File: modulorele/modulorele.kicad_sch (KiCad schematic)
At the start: 9 parts, among them J1 Rele, J2 Conn_01x03, K1 G5LE-1, Q1 SS8050

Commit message: Some changes in arduino board.
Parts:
- removed J1: Rele, TerminalBlock_Phoenix:TerminalBlock_Phoenix_MKDS-1,5-3-5.08_1x03_P5.08mm_Horizontal, symbol Connector:Screw_Terminal_01x03
- removed J2: Conn_01x03, Connector_PinHeader_2.54mm:PinHeader_1x03_P2.54mm_Vertical, symbol Connector_Generic:Conn_01x03
- added J15: Conn_01x01, Connector_PinHeader_2.54mm:PinHeader_1x01_P2.54mm_Vertical, symbol Connector_Generic:Conn_01x01
- added JP3: ~, Jumper:SolderJumper-2_P1.3mm_Bridged_RoundedPad1.0x1.5mm, symbol Jumper:SolderJumper_2_Bridged
- renumbered D1 to D5, D2 to D6, Q1 to Q3, R3 to R13, R2 to R14, R1 to R15
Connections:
- net at R13.1, R15.1: now also JP3.2 (B)
- net +12V renamed 12V
- net com renamed COM
- net na renamed NA
- net nf renamed NF
- new net INPUT: J15.1 (Pin_1), JP3.1 (A)

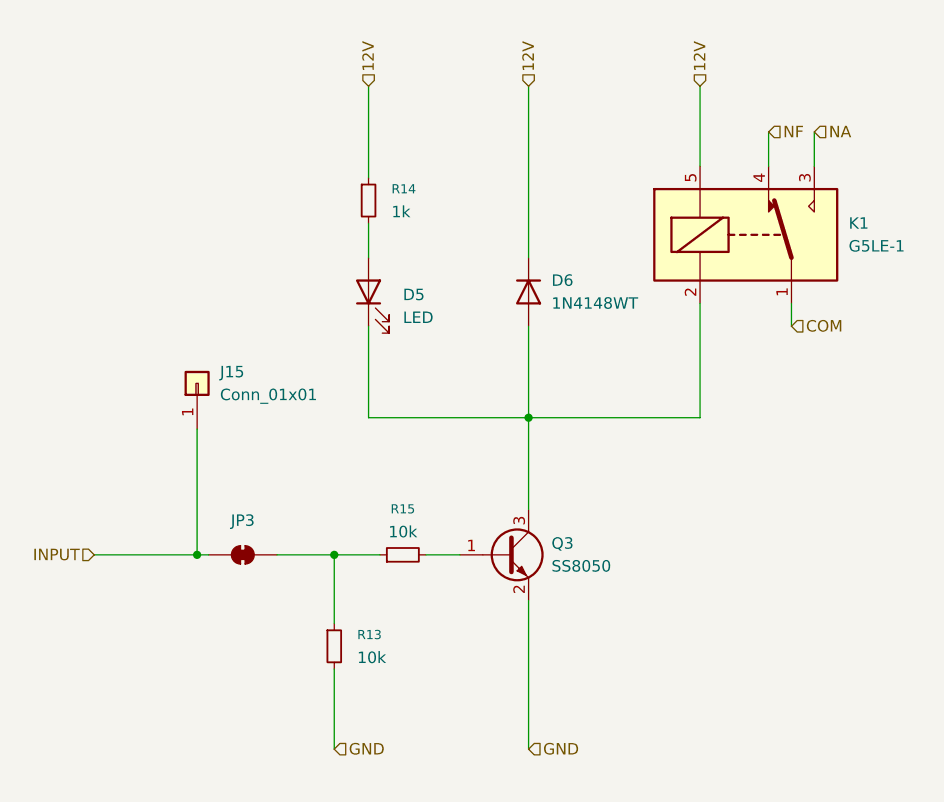
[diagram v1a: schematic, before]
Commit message: Added all components to arduino pcb.
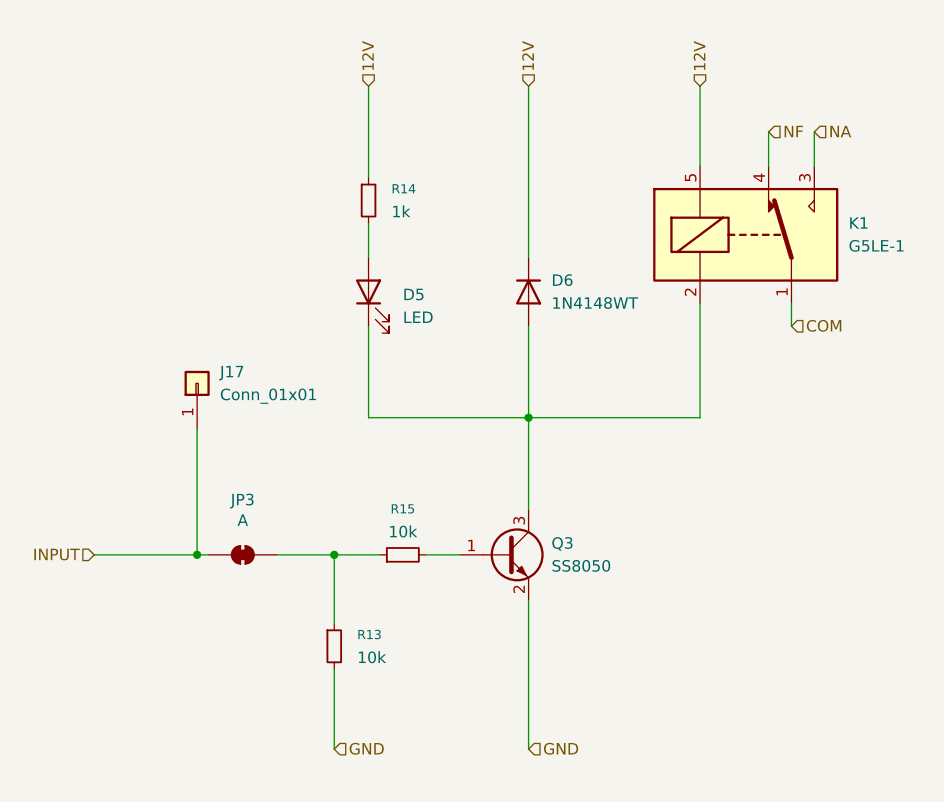
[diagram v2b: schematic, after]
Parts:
- JP3: value ~ -> A
- R13, R14, R15: footprint Resistor_SMD:R_0805_2012Metric -> Resistor_SMD:R_0805_2012Metric_Pad1.20x1.40mm_HandSolder
- renumbered J15 to J17
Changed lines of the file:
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@@
 		(dnp no)
 		(fields_autoplaced yes)
-		(property "Reference" "J15"
+		(property "Reference" "J17"
 			(at 57.15 66.0399 90)
 			(effects
@@
 			(project "Arduino"
 				(path "/b1260de1-9c48-4b08-a759-f31e40d6183e/6d409481-8893-4a65-ac5a-8215d51ff4b9/2c4cc56f-8712-443e-bcef-d2b6de1486c0"
+					(reference "J19")
+					(unit 1)
+				)
+				(path "/b1260de1-9c48-4b08-a759-f31e40d6183e/6d409481-8893-4a65-ac5a-8215d51ff4b9/4a654f2d-0a20-4954-8c37-0a9e1e731e6d"
+					(reference "J18")
+					(unit 1)
+				)
+				(path "/b1260de1-9c48-4b08-a759-f31e40d6183e/6d409481-8893-4a65-ac5a-8215d51ff4b9/7c0386ab-ad55-49ca-9208-412e4006b70e"
 					(reference "J17")
 					(unit 1)
 				)
-				(path "/b1260de1-9c48-4b08-a759-f31e40d6183e/6d409481-8893-4a65-ac5a-8215d51ff4b9/4a654f2d-0a20-4954-8c37-0a9e1e731e6d"
-					(reference "J16")
-					(unit 1)
-				)
-				(path "/b1260de1-9c48-4b08-a759-f31e40d6183e/6d409481-8893-4a65-ac5a-8215d51ff4b9/7c0386ab-ad55-49ca-9208-412e4006b70e"
-					(reference "J15")
-					(unit 1)
-				)
-				(path "/b1260de1-9c48-4b08-a759-f31e40d6183e/6d409481-8893-4a65-ac5a-8215d51ff4b9/cd925d39-8883-46ed-ba4c-9b4976049c05"
-					(reference "J18")
+				(path "/b1260de1-9c48-4b08-a759-f31e40d6183e/6d409481-8893-4a65-ac5a-8215d51ff4b9/cd925d39-8883-46ed-ba4c-9b4976049c05"
+					(reference "J26")
 					(unit 1)
 				)
@@
 			)
 		)
-		(property "Footprint" "Resistor_SMD:R_0805_2012Metric"
+		(property "Footprint" "Resistor_SMD:R_0805_2012Metric_Pad1.20x1.40mm_HandSolder"
 			(at 69.85 96.52 0)
 			(effects
@@
 				)
 				(path "/b1260de1-9c48-4b08-a759-f31e40d6183e/6d409481-8893-4a65-ac5a-8215d51ff4b9/cd925d39-8883-46ed-ba4c-9b4976049c05"
-					(reference "R22")
+					(reference "R28")
 					(unit 1)
 				)
@@
 				)
 				(path "/b1260de1-9c48-4b08-a759-f31e40d6183e/6d409481-8893-4a65-ac5a-8215d51ff4b9/cd925d39-8883-46ed-ba4c-9b4976049c05"
-					(reference "D11")
+					(reference "D15")
 					(unit 1)
 				)
@@
 			)
 		)
-		(property "Footprint" "Resistor_SMD:R_0805_2012Metric"
+		(property "Footprint" "Resistor_SMD:R_0805_2012Metric_Pad1.20x1.40mm_HandSolder"
 			(at 77.47 86.36 0)
 			(effects
@@
 				)
 				(path "/b1260de1-9c48-4b08-a759-f31e40d6183e/6d409481-8893-4a65-ac5a-8215d51ff4b9/cd925d39-8883-46ed-ba4c-9b4976049c05"
-					(reference "R24")
+					(reference "R30")
 					(unit 1)
 				)
@@
 				)
 				(path "/b1260de1-9c48-4b08-a759-f31e40d6183e/6d409481-8893-4a65-ac5a-8215d51ff4b9/cd925d39-8883-46ed-ba4c-9b4976049c05"
-					(reference "D12")
+					(reference "D16")
 					(unit 1)
 				)
@@
 		(dnp no)
 		(property "Reference" "JP3"
-			(at 59.69 82.55 0)
-			(effects
-				(font
-					(size 1.27 1.27)
-				)
-			)
-		)
-		(property "Value" "~"
+			(at 59.69 80.264 0)
+			(effects
+				(font
+					(size 1.27 1.27)
+				)
+			)
+		)
+		(property "Value" "A"
 			(at 59.69 82.55 0)
 			(effects
@@
 				)
 				(path "/b1260de1-9c48-4b08-a759-f31e40d6183e/6d409481-8893-4a65-ac5a-8215d51ff4b9/cd925d39-8883-46ed-ba4c-9b4976049c05"
-					(reference "JP6")
+					(reference "JP10")
 					(unit 1)
 				)
@@
 			)
 		)
-		(property "Footprint" "Resistor_SMD:R_0805_2012Metric"
+		(property "Footprint" "Resistor_SMD:R_0805_2012Metric_Pad1.20x1.40mm_HandSolder"
 			(at 73.66 46.99 0)
 			(effects
@@
 				)
 				(path "/b1260de1-9c48-4b08-a759-f31e40d6183e/6d409481-8893-4a65-ac5a-8215d51ff4b9/cd925d39-8883-46ed-ba4c-9b4976049c05"
-					(reference "R23")
-					(unit 1)
-				)
+					(reference "R29")
+					(unit 1)
+				)

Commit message: First version from PCB schematic.
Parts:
- removed D6: 1N4148WT, Diode_SMD:D_SOD-523, symbol Diode:1N4148WT
- added D6: 1N4007, Diode_SMD:D_SMA, symbol Diode:1N4007
- renumbered JP3 to JP4
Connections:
- net at D5.1 (K), K1.2, Q3.3 (C): now also D6.2 (A)
- net 12V renamed +12V
- net +12V: now also D6.1 (K)
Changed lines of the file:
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@@
 		)
 	)
-	(hierarchical_label "12V"
+	(hierarchical_label "+12V"
 		(shape input)
 		(at 110.49 34.29 90)
@@
 		)
 	)
-	(hierarchical_label "12V"
+	(hierarchical_label "+12V"
 		(shape input)
 		(at 73.66 34.29 90)
@@
 		)
 	)
-	(hierarchical_label "12V"
+	(hierarchical_label "+12V"
 		(shape input)
 		(at 91.44 34.29 90)
@@
 					(unit 1)
 				)
-				(path "/b1260de1-9c48-4b08-a759-f31e40d6183e/6d409481-8893-4a65-ac5a-8215d51ff4b9/7c0386ab-ad55-49ca-9208-412e4006b70e"
+				(path "/b1260de1-9c48-4b08-a759-f31e40d6183e/6d409481-8893-4a65-ac5a-8215d51ff4b9/95d6ed7c-668f-45ec-9d3e-e04d0bc610f9"
 					(reference "J17")
 					(unit 1)
@@
 					(unit 1)
 				)
-				(path "/b1260de1-9c48-4b08-a759-f31e40d6183e/6d409481-8893-4a65-ac5a-8215d51ff4b9/7c0386ab-ad55-49ca-9208-412e4006b70e"
+				(path "/b1260de1-9c48-4b08-a759-f31e40d6183e/6d409481-8893-4a65-ac5a-8215d51ff4b9/95d6ed7c-668f-45ec-9d3e-e04d0bc610f9"
 					(reference "R13")
 					(unit 1)
@@
 					(unit 1)
 				)
-				(path "/b1260de1-9c48-4b08-a759-f31e40d6183e/6d409481-8893-4a65-ac5a-8215d51ff4b9/7c0386ab-ad55-49ca-9208-412e4006b70e"
+				(path "/b1260de1-9c48-4b08-a759-f31e40d6183e/6d409481-8893-4a65-ac5a-8215d51ff4b9/95d6ed7c-668f-45ec-9d3e-e04d0bc610f9"
 					(reference "D5")
 					(unit 1)
@@
 				(path "/b1260de1-9c48-4b08-a759-f31e40d6183e/6d409481-8893-4a65-ac5a-8215d51ff4b9/cd925d39-8883-46ed-ba4c-9b4976049c05"
 					(reference "D15")
+					(unit 1)
+				)
+			)
+		)
+	)
+	(symbol
+		(lib_id "Diode:1N4007")
+		(at 91.44 57.15 270)
+		(unit 1)
+		(exclude_from_sim no)
+		(in_bom yes)
+		(on_board yes)
+		(dnp no)
+		(fields_autoplaced yes)
+		(property "Reference" "D6"
+			(at 93.98 55.8799 90)
+			(effects
+				(font
+					(size 1.27 1.27)
+				)
+				(justify left)
+			)
+		)
+		(property "Value" "1N4007"
+			(at 93.98 58.4199 90)
+			(effects
+				(font
+					(size 1.27 1.27)
+				)
+				(justify left)
+			)
+		)
+		(property "Footprint" "Diode_SMD:D_SMA"
+			(at 86.995 57.15 0)
+			(effects
+				(font
+					(size 1.27 1.27)
+				)
+				(hide yes)
+			)
+		)
+		(property "Datasheet" "http://www.vishay.com/docs/88503/1n4001.pdf"
+			(at 91.44 57.15 0)
+			(effects
+				(font
+					(size 1.27 1.27)
+				)
+				(hide yes)
+			)
+		)
+		(property "Description" "1000V 1A General Purpose Rectifier Diode, DO-41"
+			(at 91.44 57.15 0)
+			(effects
+				(font
+					(size 1.27 1.27)
+				)
+				(hide yes)
+			)
+		)
+		(property "Sim.Device" "D"
+			(at 91.44 57.15 0)
+			(effects
+				(font
+					(size 1.27 1.27)
+				)
+				(hide yes)
+			)
+		)
+		(property "Sim.Pins" "1=K 2=A"
+			(at 91.44 57.15 0)
+			(effects
+				(font
+					(size 1.27 1.27)
+				)
+				(hide yes)
+			)
+		)
+		(pin "2"
+		)
+		(pin "1"
+		)
+		(instances
+			(project "Arduino"
+				(path "/b1260de1-9c48-4b08-a759-f31e40d6183e/6d409481-8893-4a65-ac5a-8215d51ff4b9/2c4cc56f-8712-443e-bcef-d2b6de1486c0"
+					(reference "D10")
+					(unit 1)
+				)
+				(path "/b1260de1-9c48-4b08-a759-f31e40d6183e/6d409481-8893-4a65-ac5a-8215d51ff4b9/4a654f2d-0a20-4954-8c37-0a9e1e731e6d"
+					(reference "D8")
+					(unit 1)
+				)
+				(path "/b1260de1-9c48-4b08-a759-f31e40d6183e/6d409481-8893-4a65-ac5a-8215d51ff4b9/95d6ed7c-668f-45ec-9d3e-e04d0bc610f9"
+					(reference "D6")
+					(unit 1)
+				)
+				(path "/b1260de1-9c48-4b08-a759-f31e40d6183e/6d409481-8893-4a65-ac5a-8215d51ff4b9/cd925d39-8883-46ed-ba4c-9b4976049c05"
+					(reference "D16")
 					(unit 1)
 				)
@@
 					(unit 1)
 				)
-				(path "/b1260de1-9c48-4b08-a759-f31e40d6183e/6d409481-8893-4a65-ac5a-8215d51ff4b9/7c0386ab-ad55-49ca-9208-412e4006b70e"
+				(path "/b1260de1-9c48-4b08-a759-f31e40d6183e/6d409481-8893-4a65-ac5a-8215d51ff4b9/95d6ed7c-668f-45ec-9d3e-e04d0bc610f9"
 					(reference "Q3")
 					(unit 1)
@@
 					(unit 1)
 				)
-				(path "/b1260de1-9c48-4b08-a759-f31e40d6183e/6d409481-8893-4a65-ac5a-8215d51ff4b9/7c0386ab-ad55-49ca-9208-412e4006b70e"
+				(path "/b1260de1-9c48-4b08-a759-f31e40d6183e/6d409481-8893-4a65-ac5a-8215d51ff4b9/95d6ed7c-668f-45ec-9d3e-e04d0bc610f9"
 					(reference "R15")
 					(unit 1)
@@
 				(path "/b1260de1-9c48-4b08-a759-f31e40d6183e/6d409481-8893-4a65-ac5a-8215d51ff4b9/cd925d39-8883-46ed-ba4c-9b4976049c05"
 					(reference "R30")
-					(unit 1)
-				)
-			)
-		)
-	)
-	(symbol
-		(lib_id "Diode:1N4148WT")
-		(at 91.44 57.15 270)
-		(unit 1)
-		(exclude_from_sim no)
-		(in_bom yes)
-		(on_board yes)
-		(dnp no)
-		(fields_autoplaced yes)
-		(property "Reference" "D6"
-			(at 93.98 55.8799 90)
-			(effects
-				(font
-					(size 1.27 1.27)
-				)
-				(justify left)
-			)
-		)
-		(property "Value" "1N4148WT"
-			(at 93.98 58.4199 90)
-			(effects
-				(font
-					(size 1.27 1.27)
-				)
-				(justify left)
-			)
-		)
-		(property "Footprint" "Diode_SMD:D_SOD-523"
-			(at 86.995 57.15 0)
-			(effects
-				(font
-					(size 1.27 1.27)
-				)
-				(hide yes)
-			)
-		)
-		(property "Datasheet" "https://www.diodes.com/assets/Datasheets/ds30396.pdf"
-			(at 91.44 57.15 0)
-			(effects
-				(font
-					(size 1.27 1.27)
-				)
-				(hide yes)
-			)
-		)
-		(property "Description" "75V 0.15A Fast switching Diode, SOD-523"
-			(at 91.44 57.15 0)
-			(effects
-				(font
-					(size 1.27 1.27)
-				)
-				(hide yes)
-			)
-		)
-		(property "Sim.Device" "D"
-			(at 91.44 57.15 0)
-			(effects
-				(font
-					(size 1.27 1.27)
-				)
-				(hide yes)
-			)
-		)
-		(property "Sim.Pins" "1=K 2=A"
-			(at 91.44 57.15 0)
-			(effects
-				(font
-					(size 1.27 1.27)
-				)
-				(hide yes)
-			)
-		)
-		(pin "1"
-		)
-		(pin "2"
-		)
-		(instances
-			(project "Arduino"
-				(path "/b1260de1-9c48-4b08-a759-f31e40d6183e/6d409481-8893-4a65-ac5a-8215d51ff4b9/2c4cc56f-8712-443e-bcef-d2b6de1486c0"
-					(reference "D10")
-					(unit 1)
-				)
-				(path "/b1260de1-9c48-4b08-a759-f31e40d6183e/6d409481-8893-4a65-ac5a-8215d51ff4b9/4a654f2d-0a20-4954-8c37-0a9e1e731e6d"
-					(reference "D8")
-					(unit 1)
-				)
-				(path "/b1260de1-9c48-4b08-a759-f31e40d6183e/6d409481-8893-4a65-ac5a-8215d51ff4b9/7c0386ab-ad55-49ca-9208-412e4006b70e"
-					(reference "D6")
-					(unit 1)
-				)
-				(path "/b1260de1-9c48-4b08-a759-f31e40d6183e/6d409481-8893-4a65-ac5a-8215d51ff4b9/cd925d39-8883-46ed-ba4c-9b4976049c05"
-					(reference "D16")
 					(unit 1)
 				)
@@
 		(on_board yes)
 		(dnp no)
-		(property "Reference" "JP3"
+		(property "Reference" "JP4"
 			(at 59.69 80.264 0)
 			(effects
@@
 			(project "Arduino"
 				(path "/b1260de1-9c48-4b08-a759-f31e40d6183e/6d409481-8893-4a65-ac5a-8215d51ff4b9/2c4cc56f-8712-443e-bcef-d2b6de1486c0"
+					(reference "JP6")
+					(unit 1)
+				)
+				(path "/b1260de1-9c48-4b08-a759-f31e40d6183e/6d409481-8893-4a65-ac5a-8215d51ff4b9/4a654f2d-0a20-4954-8c37-0a9e1e731e6d"
 					(reference "JP5")
 					(unit 1)
 				)
-				(path "/b1260de1-9c48-4b08-a759-f31e40d6183e/6d409481-8893-4a65-ac5a-8215d51ff4b9/4a654f2d-0a20-4954-8c37-0a9e1e731e6d"
+				(path "/b1260de1-9c48-4b08-a759-f31e40d6183e/6d409481-8893-4a65-ac5a-8215d51ff4b9/95d6ed7c-668f-45ec-9d3e-e04d0bc610f9"
 					(reference "JP4")
 					(unit 1)
 				)
-				(path "/b1260de1-9c48-4b08-a759-f31e40d6183e/6d409481-8893-4a65-ac5a-8215d51ff4b9/7c0386ab-ad55-49ca-9208-412e4006b70e"
-					(reference "JP3")
-					(unit 1)
-				)
 				(path "/b1260de1-9c48-4b08-a759-f31e40d6183e/6d409481-8893-4a65-ac5a-8215d51ff4b9/cd925d39-8883-46ed-ba4c-9b4976049c05"
-					(reference "JP10")
+					(reference "JP11")
 					(unit 1)
 				)
@@
 					(unit 1)
 				)
-				(path "/b1260de1-9c48-4b08-a759-f31e40d6183e/6d409481-8893-4a65-ac5a-8215d51ff4b9/7c0386ab-ad55-49ca-9208-412e4006b70e"
+				(path "/b1260de1-9c48-4b08-a759-f31e40d6183e/6d409481-8893-4a65-ac5a-8215d51ff4b9/95d6ed7c-668f-45ec-9d3e-e04d0bc610f9"
 					(reference "R14")
 					(unit 1)
@@
 					(unit 1)
 				)
-				(path "/b1260de1-9c48-4b08-a759-f31e40d6183e/6d409481-8893-4a65-ac5a-8215d51ff4b9/7c0386ab-ad55-49ca-9208-412e4006b70e"
+				(path "/b1260de1-9c48-4b08-a759-f31e40d6183e/6d409481-8893-4a65-ac5a-8215d51ff4b9/95d6ed7c-668f-45ec-9d3e-e04d0bc610f9"
 					(reference "K1")
 					(unit 1)
